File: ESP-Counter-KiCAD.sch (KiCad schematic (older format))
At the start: 44 parts, among them J1 Digital_IP, J2 Motor_Ctrl, J3 LED_Indicator, J4 ADC, J5 24V_Input, K2 G2RL-1-DC24, K5 G2RL-1-DC24, U1 ESP_12E_J1, U10 VO615A, U11 AT25xxx-MA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

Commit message: Routing completed - Second iteration
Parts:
- added H1, H2, H3, H4: ., MountingHole:MountingHole_3.2mm_M3, symbol Mechanical:MountingHole
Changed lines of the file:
@@
 	1500 5248 1656 5248
 NoConn ~ 1500 5648
+$Comp
+L Mechanical:MountingHole H1
+U 1 1 6027DF3A
+P 10408 5794
+F 0 "H1" H 10508 5840 50  0000 L CNN
+F 1 "." H 10508 5749 50  0000 L CNN
+F 2 "MountingHole:MountingHole_3.2mm_M3" H 10408 5794 50  0001 C CNN
+F 3 "~" H 10408 5794 50  0001 C CNN
+	1    10408 5794
+	1    0    0    -1
+$EndComp
+$Comp
+L Mechanical:MountingHole H2
+U 1 1 6027E472
+P 10410 5972
+F 0 "H2" H 10510 6018 50  0000 L CNN
+F 1 "." H 10510 5927 50  0000 L CNN
+F 2 "MountingHole:MountingHole_3.2mm_M3" H 10410 5972 50  0001 C CNN
+F 3 "~" H 10410 5972 50  0001 C CNN
+	1    10410 5972
+	1    0    0    -1
+$EndComp
+$Comp
+L Mechanical:MountingHole H3
+U 1 1 6027EA02
+P 10416 6150
+F 0 "H3" H 10516 6196 50  0000 L CNN
+F 1 "." H 10516 6105 50  0000 L CNN
+F 2 "MountingHole:MountingHole_3.2mm_M3" H 10416 6150 50  0001 C CNN
+F 3 "~" H 10416 6150 50  0001 C CNN
+	1    10416 6150
+	1    0    0    -1
+$EndComp
+$Comp
+L Mechanical:MountingHole H4
+U 1 1 6027EBF0
+P 10420 6332
+F 0 "H4" H 10520 6378 50  0000 L CNN
+F 1 "." H 10520 6287 50  0000 L CNN
+F 2 "MountingHole:MountingHole_3.2mm_M3" H 10420 6332 50  0001 C CNN
+F 3 "~" H 10420 6332 50  0001 C CNN
+	1    10420 6332
+	1    0    0    -1
+$EndComp
 $EndSCHEMATC

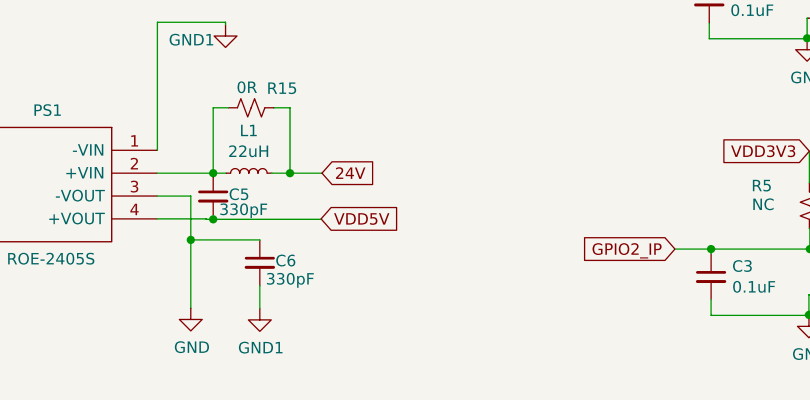
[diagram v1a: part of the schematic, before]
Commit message: 220uF Cap added at 5V
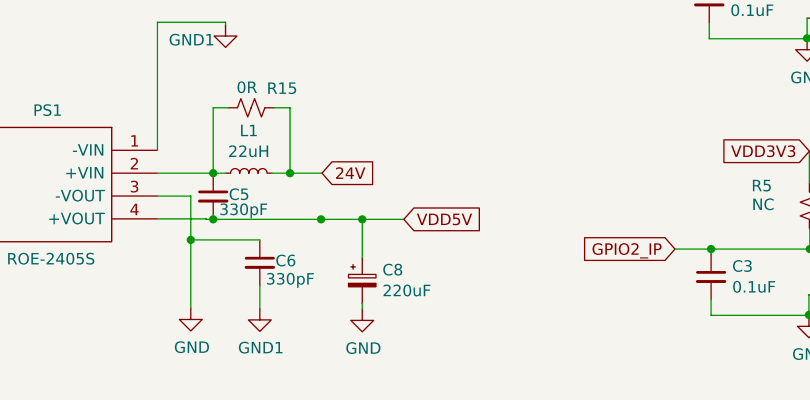
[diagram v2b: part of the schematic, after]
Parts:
- added C8: 220uF, Capacitor_THT:CP_Radial_D5.0mm_P2.00mm, symbol Device:CP_Small
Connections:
- wire segments 204 -> 208
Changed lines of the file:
@@
 Wire Wire Line
 	1986 6828 2066 6828
-Text GLabel 2202 7028 2    50   Input ~ 0
+Text GLabel 2564 7030 2    50   Input ~ 0
 VDD5V
 $Comp
@@
 	1    0    0    -1
 $EndComp
+$Comp
+L Device:CP_Small C8
+U 1 1 60275CD2
+P 2382 7298
+F 0 "C8" H 2470 7344 50  0000 L CNN
+F 1 "220uF" H 2470 7253 50  0000 L CNN
+F 2 "Capacitor_THT:CP_Radial_D5.0mm_P2.00mm" H 2382 7298 50  0001 C CNN
+F 3 "~" H 2382 7298 50  0001 C CNN
+	1    2382 7298
+	1    0    0    -1
+$EndComp
+Wire Wire Line
+	2202 7030 2382 7030
+Connection ~ 2202 7030
+Wire Wire Line
+	2382 7198 2382 7030
+Connection ~ 2382 7030
+Wire Wire Line
+	2382 7030 2564 7030
+$Comp
+L power:GND #PWR06
+U 1 1 6028F588
+P 2382 7422
+F 0 "#PWR06" H 2382 7172 50  0001 C CNN
+F 1 "GND" H 2387 7249 50  0000 C CNN
+F 2 "" H 2382 7422 50  0001 C CNN
+F 3 "" H 2382 7422 50  0001 C CNN
+	1    2382 7422
+	1    0    0    -1
+$EndComp
+Wire Wire Line
+	2382 7422 2382 7398
 $EndSCHEMATC
